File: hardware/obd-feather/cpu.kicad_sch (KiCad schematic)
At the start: 3 parts, among them U1 Adafruit Feather STM32F405 Ex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

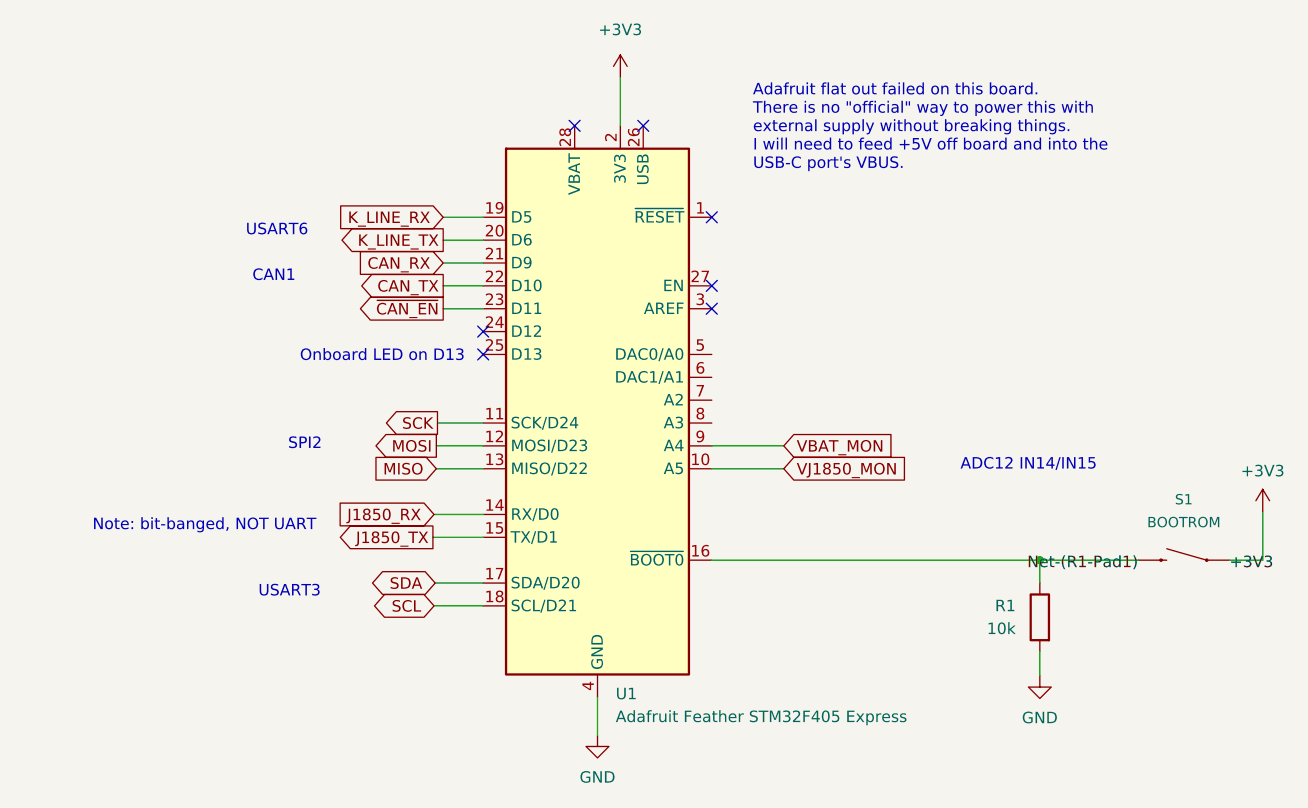
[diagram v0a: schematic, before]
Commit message: Added in KLine support (ISO9141 and ISO-14230/KWP)
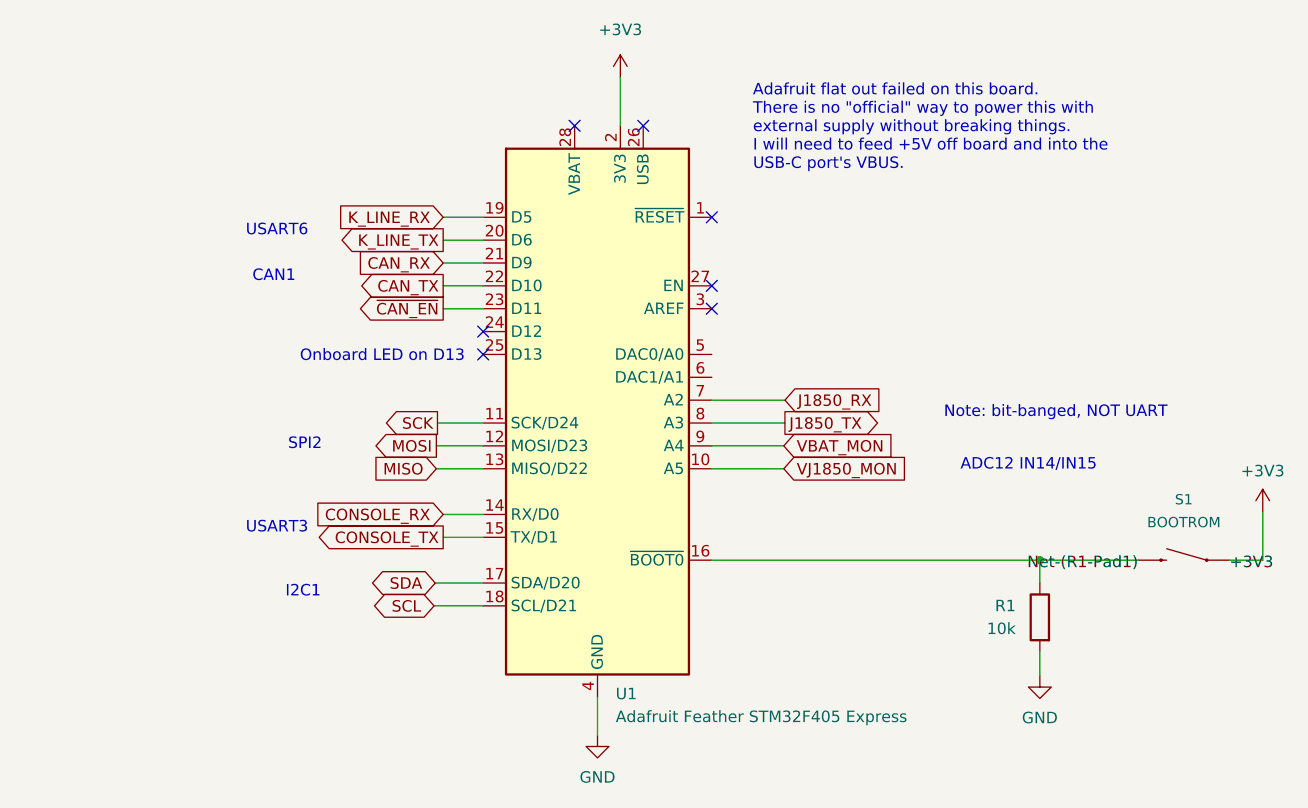
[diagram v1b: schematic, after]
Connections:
- net J1850_RX: now also U1.7 (A2); no longer U1.14 (RX/D0)
- net J1850_TX: now also U1.8 (A3); no longer U1.15 (TX/D1)
- new net CONSOLE_RX: U1.14 (RX/D0)
- new net CONSOLE_TX: U1.15 (TX/D1)
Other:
- note added: "I2C1"
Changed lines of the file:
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@@
     (stroke (width 0) (type default) (color 0 0 0 0))
   )
-  (wire (pts (xy 119.38 103.251) (xy 124.968 103.251))
+  (wire (pts (xy 120.523 100.711) (xy 124.968 100.711))
     (stroke (width 0) (type default) (color 0 0 0 0))
   )
@@
     (stroke (width 0) (type default) (color 0 0 0 0))
   )
+  (wire (pts (xy 158.496 90.551) (xy 150.368 90.551))
+    (stroke (width 0) (type default) (color 0 0 0 0))
+  )
   (wire (pts (xy 140.208 52.197) (xy 140.208 57.531))
     (stroke (width 0) (type default) (color 0 0 0 0))
@@
     (stroke (width 0) (type default) (color 0 0 0 0))
   )
-  (wire (pts (xy 119.507 100.711) (xy 124.968 100.711))
+  (wire (pts (xy 119.507 110.871) (xy 124.968 110.871))
     (stroke (width 0) (type default) (color 0 0 0 0))
   )
-  (wire (pts (xy 119.507 110.871) (xy 124.968 110.871))
+  (wire (pts (xy 120.523 103.251) (xy 124.968 103.251))
     (stroke (width 0) (type default) (color 0 0 0 0))
   )
@@
     (stroke (width 0) (type default) (color 0 0 0 0))
   )
+  (wire (pts (xy 158.496 88.011) (xy 150.368 88.011))
+    (stroke (width 0) (type default) (color 0 0 0 0))
+  )
   (wire (pts (xy 186.817 115.951) (xy 186.817 118.618))
     (stroke (width 0) (type default) (color 0 0 0 0))
   )
-  (text "Note: bit-banged, NOT UART" (at 106.426 102.743 180)
+  (text "USART3" (at 105.537 102.997 180)
     (effects (font (size 1.27 1.27)) (justify right bottom))
   )
@@
     (effects (font (size 1.27 1.27)) (justify left bottom))
   )
-  (text "USART3" (at 106.934 110.109 180)
+  (text "I2C1" (at 106.934 110.109 180)
     (effects (font (size 1.27 1.27)) (justify right bottom))
+  )
+  (text "Note: bit-banged, NOT UART" (at 176.149 90.17 0)
+    (effects (font (size 1.27 1.27)) (justify left bottom))
   )
   (text "SPI2" (at 107.061 93.726 180)
@@
     )
   )
+  (global_label "J1850_TX" (shape output) (at 158.496 90.551 0) (fields_autoplaced)
+    (effects (font (size 1.27 1.27)) (justify left))
+    (property "Intersheet References" "${INTERSHEET_REFS}" (id 0) (at 169.8596 90.6304 0)
+      (effects (font (size 1.27 1.27)) (justify left) hide)
+    )
+  )
   (global_label "SCL" (shape bidirectional) (at 119.507 110.871 180) (fields_autoplaced)
     (effects (font (size 1.27 1.27)) (justify right))
     (property "Intersheet References" "${INTERSHEET_REFS}" (id 0) (at 113.5863 110.7916 0)
-      (effects (font (size 1.27 1.27)) (justify right) hide)
-    )
-  )
-  (global_label "J1850_RX" (shape input) (at 119.507 100.711 180) (fields_autoplaced)
-    (effects (font (size 1.27 1.27)) (justify right))
-    (property "Intersheet References" "${INTERSHEET_REFS}" (id 0) (at 107.841 100.7904 0)
       (effects (font (size 1.27 1.27)) (justify right) hide)
     )
@@
     )
   )
-  (global_label "J1850_TX" (shape output) (at 119.38 103.251 180) (fields_autoplaced)
+  (global_label "CONSOLE_TX" (shape output) (at 120.523 103.251 180) (fields_autoplaced)
     (effects (font (size 1.27 1.27)) (justify right))
-    (property "Intersheet References" "${INTERSHEET_REFS}" (id 0) (at 108.0164 103.3304 0)
+    (property "Intersheet References" "${INTERSHEET_REFS}" (id 0) (at 106.317 103.1716 0)
       (effects (font (size 1.27 1.27)) (justify right) hide)
+    )
+  )
+  (global_label "J1850_RX" (shape input) (at 158.496 88.011 0) (fields_autoplaced)
+    (effects (font (size 1.27 1.27)) (justify left))
+    (property "Intersheet References" "${INTERSHEET_REFS}" (id 0) (at 170.162 88.0904 0)
+      (effects (font (size 1.27 1.27)) (justify left) hide)
     )
   )
@@
       (effects (font (size 1.27 1.27)) (justify right) hide)
     )
+  )
+  (global_label "CONSOLE_RX" (shape input) (at 120.523 100.711 180) (fields_autoplaced)
+    (effects (font (size 1.27 1.27)) (justify right))
+    (property "Intersheet References" "${INTERSHEET_REFS}" (id 0) (at 106.0147 100.6316 0)
+      (effects (font (size 1.27 1.27)) (justify right) hide)
+    )
